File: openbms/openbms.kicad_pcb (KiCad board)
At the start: 4 copper layers, 68.4 x 52.4 mm, 220 parts, among them J1 3-pin JST connector, J2 TagConnect_TC2030, J3 8-pin JST connector, J4 2-pin JST connector, J5 XT60PW-M connector, J6 XT60PW-F connector, J7 7-pin JST connector, Q1 NTMFS5C612NLT1G, Q2 NTMFS5C612NLT1G, Q3 BSS84AKW,115, Q4 2N7002KW, Q5 2N7002KW, Q6 BSS84AKW,115, Q7 2N7002KW, SW1 SW_Push, U1 DMP68D1LVQ-7, U10 DMP68D1LVQ-7, U11 DMN601VK-7, U12 DMN601VK-7, U13 DMN601VK-7, U14 DMN601VK-7, U15 STM32L431CCUx, U16 TCAN3413DRBR, U17 32kbit EEPROM memory, U18 DMP68D1LVQ-7, U19 TPS12000QDGXRQ1, U2 DMP68D1LVQ-7, U20 LMZM23600V3, U22 DMN601VK-7, U3 DMN601VK-7, U4 DMP68D1LVQ-7, U5 ADS131M08xPBS, U6 DMP68D1LVQ-7, U7 DMN601VK-7, U8 DMP68D1LVQ-7, U9 DMP68D1LVQ-7, Y1 8.192MHz, Y2 8MHz

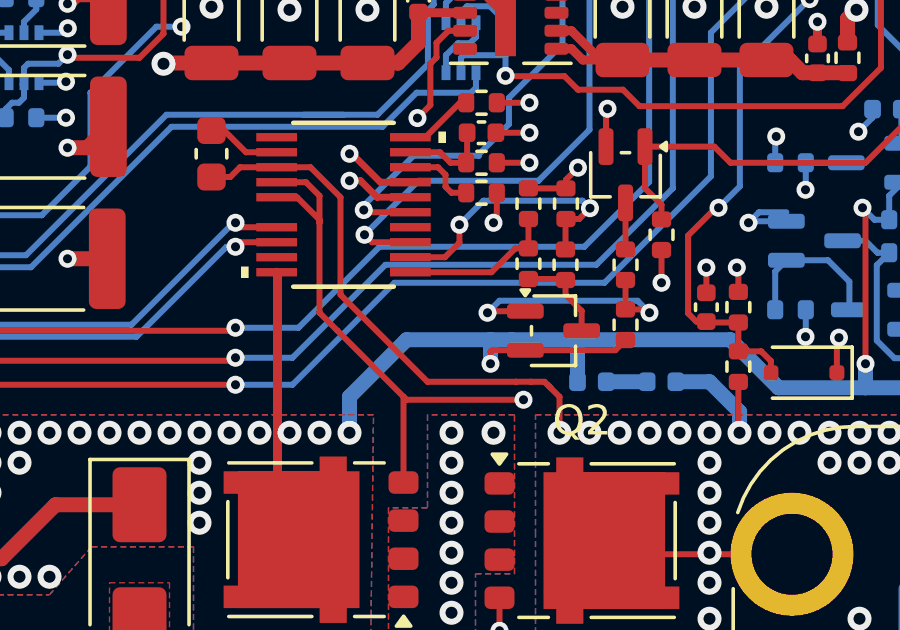
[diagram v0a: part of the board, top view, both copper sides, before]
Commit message: Polygon zone fixed, SRC net in FET fixed
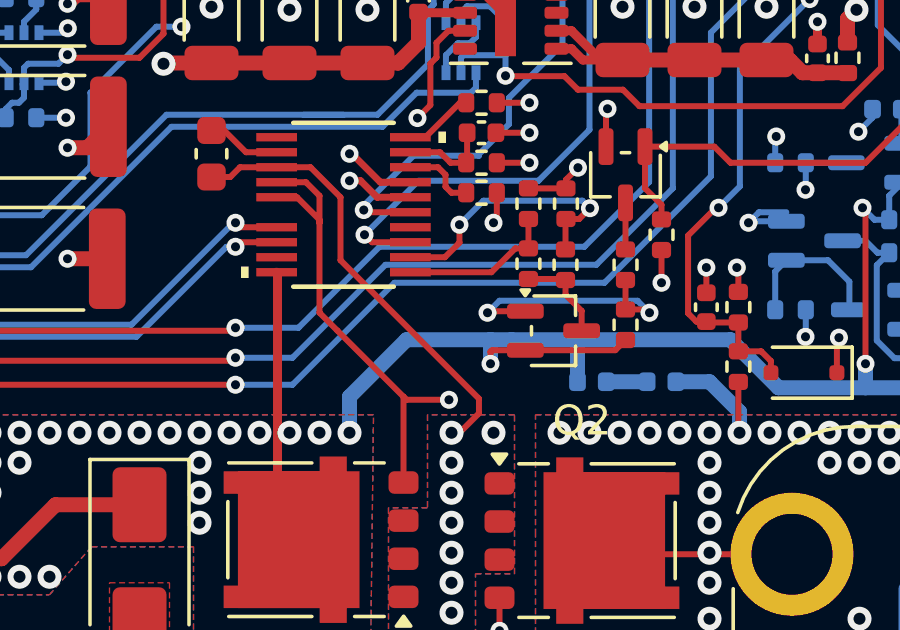
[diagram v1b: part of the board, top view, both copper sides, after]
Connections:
- C33 pad 2: /FETs/SYS_VCC -> Net-(U19-SRC)
- Q1 pad 1: Net-(Q1-S-Pad1) -> Net-(U19-SRC)
- Q1 pad 2: Net-(Q1-S-Pad1) -> Net-(U19-SRC)
- Q1 pad 3: Net-(Q1-S-Pad1) -> Net-(U19-SRC)
- Q2 pad 1: Net-(Q1-S-Pad1) -> Net-(U19-SRC)
- Q2 pad 2: Net-(Q1-S-Pad1) -> Net-(U19-SRC)
- Q2 pad 3: Net-(Q1-S-Pad1) -> Net-(U19-SRC)
- U19 pad 13: /FETs/SYS_VCC -> Net-(U19-SRC)
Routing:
- net /FETs/SYS_VCC: track 43.9 -> 25.7 mm
- net Net-(U19-SRC): track 0.00 -> 15.1 mm, vias 0 -> 10
- net Net-(Q1-S-Pad1): vias 10 -> 0
- added copper zone on B.Cu, net Net-(U19-SRC)
- added copper zone on F.Cu, net Net-(U19-SRC)
- added copper zone on In1.Cu, net Net-(U19-SRC)
- added copper zone on In2.Cu, net Net-(U19-SRC)
- removed copper zone on B.Cu, net Net-(Q1-S-Pad1)
- removed copper zone on F.Cu, net Net-(Q1-S-Pad1)
- removed copper zone on In1.Cu, net Net-(Q1-S-Pad1)
- removed copper zone on In2.Cu, net Net-(Q1-S-Pad1)
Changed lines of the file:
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@@
 	(net 62 "/MCU/NTC")
 	(net 63 "/ADC/BATT_CS_POS")
-	(net 64 "Net-(Q1-S-Pad1)")
+	(net 64 "Net-(U19-SRC)")
 	(net 65 "Net-(Q1-G)")
 	(net 66 "Net-(Q3-D)")
@@
 			(layers "F.Cu" "F.Mask" "F.Paste")
 			(roundrect_rratio 0.25)
-			(net 29 "/FETs/SYS_VCC")
+			(net 64 "Net-(U19-SRC)")
 			(pintype "passive")
 		)
@@
 			(size 1.3589 0.2794)
 			(layers "F.Cu" "F.Mask" "F.Paste")
-			(net 29 "/FETs/SYS_VCC")
+			(net 64 "Net-(U19-SRC)")
 			(pinfunction "SRC")
 			(pintype "output")
@@
 		(sheetname "/FETs/")
 		(sheetfile "FETs.kicad_sch")
+		(zone_connect 2)
 		(attr smd)
 		(fp_line
@@
 			(layers "F.Cu" "F.Mask" "F.Paste")
 			(roundrect_rratio 0.25)
-			(net 64 "Net-(Q1-S-Pad1)")
+			(net 64 "Net-(U19-SRC)")
 			(pinfunction "S")
 			(pintype "passive")
@@
 			(layers "F.Cu" "F.Mask" "F.Paste")
 			(roundrect_rratio 0.25)
-			(net 64 "Net-(Q1-S-Pad1)")
+			(net 64 "Net-(U19-SRC)")
 			(pinfunction "S")
 			(pintype "passive")
@@
 			(layers "F.Cu" "F.Mask" "F.Paste")
 			(roundrect_rratio 0.25)
-			(net 64 "Net-(Q1-S-Pad1)")
+			(net 64 "Net-(U19-SRC)")
 			(pinfunction "S")
 			(pintype "passive")
@@
 			(layers "F.Cu" "F.Mask" "F.Paste")
 			(roundrect_rratio 0.25)
-			(net 64 "Net-(Q1-S-Pad1)")
+			(net 64 "Net-(U19-SRC)")
 			(pinfunction "S")
 			(pintype "passive")
@@
 			(layers "F.Cu" "F.Mask" "F.Paste")
 			(roundrect_rratio 0.25)
-			(net 64 "Net-(Q1-S-Pad1)")
+			(net 64 "Net-(U19-SRC)")
 			(pinfunction "S")
 			(pintype "passive")
@@
 			(layers "F.Cu" "F.Mask" "F.Paste")
 			(roundrect_rratio 0.25)
-			(net 64 "Net-(Q1-S-Pad1)")
+			(net 64 "Net-(U19-SRC)")
 			(pinfunction "S")
 			(pintype "passive")
@@
 	)
 	(segment
-		(start 106.686057 69.1345)
-		(end 106.684057 69.1365)
-		(width 0.2)
-		(layer "F.Cu")
-		(net 29)
-	)
-	(segment
 		(start 110.08225 74.885)
 		(end 109.62725 74.43)
@@
 	)
 	(segment
-		(start 107.8345 69.3355)
-		(end 107.6355 69.1365)
-		(width 0.2)
-		(layer "F.Cu")
-		(net 29)
-	)
-	(segment
-		(start 107.6355 69.1365)
-		(end 107.185943 69.1365)
-		(width 0.2)
-		(layer "F.Cu")
-		(net 29)
-	)
-	(segment
-		(start 100.8345 62.985443)
-		(end 99.834057 61.985)
-		(width 0.2)
-		(layer "F.Cu")
-		(net 29)
-	)
-	(segment
-		(start 108.135 69.636)
-		(end 107.8345 69.3355)
-		(width 0.2)
-		(layer "F.Cu")
-		(net 29)
-	)
-	(segment
-		(start 99.834057 61.985)
-		(end 98.70615 61.985)
-		(width 0.2)
-		(layer "F.Cu")
-		(net 29)
-	)
-	(segment
-		(start 97.1595 62.3105)
-		(end 96.5345 62.3105)
-		(width 0.2)
-		(layer "F.Cu")
-		(net 29)
-	)
-	(segment
-		(start 108.135 70.835)
-		(end 108.135 69.636)
-		(width 0.2)
-		(layer "F.Cu")
-		(net 29)
-	)
-	(segment
 		(start 115.885 74.885)
 		(end 110.08225 74.885)
@@
 	)
 	(segment
-		(start 107.185943 69.1365)
-		(end 107.183943 69.1345)
-		(width 0.2)
-		(layer "F.Cu")
-		(net 29)
-	)
-	(segment
 		(start 128.935 81.135)
 		(end 129.435 80.635)
@@
 	)
 	(segment
-		(start 106.684057 69.1365)
-		(end 103.7355 69.1365)
-		(width 0.2)
-		(layer "F.Cu")
-		(net 29)
-	)
-	(segment
 		(start 126.835 81.135)
 		(end 128.935 81.135)
@@
 	)
 	(segment
-		(start 100.8345 66.2355)
-		(end 100.8345 62.985443)
-		(width 0.2)
-		(layer "F.Cu")
-		(net 29)
-	)
-	(segment
-		(start 98.70615 61.985)
-		(end 97.485 61.985)
-		(width 0.2)
-		(layer "F.Cu")
-		(net 29)
-	)
-	(segment
-		(start 97.485 61.985)
-		(end 97.1595 62.3105)
-		(width 0.2)
-		(layer "F.Cu")
-		(net 29)
-	)
-	(segment
 		(start 123.735 78.035)
 		(end 126.835 81.135)
@@
 	)
 	(segment
-		(start 103.7355 69.1365)
-		(end 100.8345 66.2355)
-		(width 0.2)
-		(layer "F.Cu")
-		(net 29)
-	)
-	(segment
 		(start 114.0968 70.7968)
 		(end 114.135 70.835)
@@
 		(net 29)
 	)
-	(segment
-		(start 107.183943 69.1345)
-		(end 106.686057 69.1345)
-		(width 0.2)
-		(layer "F.Cu")
-		(net 29)
-	)
-	(segment
-		(start 107.8345 69.3355)
-		(end 107.7345 69.2355)
-		(width 0.2)
-		(layer "F.Cu")
-		(net 29)
-	)
 	(via
 		(at 118.135 78.035)
@@
 		(net 63)
 	)
+	(segment
+		(start 100.8345 62.985443)
+		(end 99.834057 61.985)
+		(width 0.2)
+		(layer "F.Cu")
+		(net 64)
+	)
+	(segment
+		(start 97.1595 62.3105)
+		(end 96.5345 62.3105)
+		(width 0.2)
+		(layer "F.Cu")
+		(net 64)
+	)
+	(segment
+		(start 104.535 70.835)
+		(end 104.8015 70.835)
+		(width 0.2)
+		(layer "F.Cu")
+		(net 64)
+	)
+	(segment
+		(start 104.8015 70.835)
+		(end 105.45 70.1865)
+		(width 0.2)
+		(layer "F.Cu")
+		(net 64)
+	)
+	(segment
+		(start 98.70615 61.985)
+		(end 97.485 61.985)
+		(width 0.2)
+		(layer "F.Cu")
+		(net 64)
+	)
+	(segment
+		(start 97.485 61.985)
+		(end 97.1595 62.3105)
+		(width 0.2)
+		(layer "F.Cu")
+		(net 64)
+	)
+	(segment
+		(start 105.45 70.1865)
+		(end 105.45 69.7)
+		(width 0.2)
+		(layer "F.Cu")
+		(net 64)
+	)
+	(segment
+		(start 105.45 69.7)
+		(end 100.8345 65.0845)
+		(width 0.2)
+		(layer "F.Cu")
+		(net 64)
+	)
+	(segment
+		(start 99.834057 61.985)
+		(end 98.70615 61.985)
+		(width 0.2)
+		(layer "F.Cu")
+		(net 64)
+	)
+	(segment
+		(start 100.8345 65.0845)
+		(end 100.8345 62.985443)
+		(width 0.2)
+		(layer "F.Cu")
+		(net 64)
+	)
 	(via
 		(at 104.535 72.835)
@@
 	)
 	(segment
-		(start 103.0355 69.7355)
-		(end 102.935 69.635)
+		(start 100.1345 62.9355)
+		(end 99.683999 62.484999)
 		(width 0.2)
 		(layer "F.Cu")
@@
 	)
 	(segment
-		(start 100.1345 62.9355)
-		(end 99.683999 62.484999)
+		(start 104.45 69.7365)
+		(end 104.449 69.7355)
 		(width 0.2)
 		(layer "F.Cu")
@@
 	)
 	(segment
-		(start 106.935 69.7355)
-		(end 103.0355 69.7355)
-		(width 0.2)
-		(layer "F.Cu")
-		(net 65)
-	)
-	(segment
 		(start 99.683999 62.484999)
 		(end 98.70615 62.484999)
@@
 	)
 	(segment
+		(start 104.449 69.7355)
+		(end 103.0355 69.7355)
+		(width 0.2)
+		(layer "F.Cu")
+		(net 65)
+	)
+	(segment
 		(start 106.135 76.335)
 		(end 106.135 77.435)
@@
 	)
 	(segment
+		(start 103.0355 69.7355)
+		(end 102.935 69.635)
+		(width 0.2)
+		(layer "F.Cu")
+		(net 65)
+	)
+	(segment
 		(start 99.384 62.985)
 		(end 100.1345 63.7355)
@@
 	)
 	(via
-		(at 106.935 69.7355)
+		(at 104.45 69.7365)
 		(size 0.6)
 		(drill 0.3)
@@
 	)
 	(segment
-		(start 106.135 72.335)
-		(end 106.135 77.435)
+		(start 106.135 77.435)
+		(end 106.135 72.265)
+		(width 0.2)
+		(layer "In1.Cu")
+		(net 65)
+	)
+	(segment
+		(start 106.135 72.265)
+		(end 106.85 71.55)
+		(width 0.2)
+		(layer "In1.Cu")
+		(net 65)
+	)
+	(segment
+		(start 106.2365 69.7365)
+		(end 104.45 69.7365)
 		(width 0.2)
 		(layer "In1.Cu")
@@
 	)
 	(segment
-		(start 106.935 69.7355)
-		(end 106.935 71.535)
+		(start 106.85 70.35)
+		(end 106.2365 69.7365)
 		(width 0.2)
 		(layer "In1.Cu")
@@
 	)
 	(segment
-		(start 106.935 71.535)
-		(end 106.135 72.335)
+		(start 106.85 71.55)
+		(end 106.85 70.35)
 		(width 0.2)
 		(layer "In1.Cu")
@@
 		(layers "F.Cu" "B.Cu" "In1.Cu" "In2.Cu")
 		(hatch none 0.5)
-		(priority 2)
 		(connect_pads thru_hole_only
 			(clearance 0.5)
@@
 	(zone
 		(net 64)
-		(net_name "Net-(Q1-S-Pad1)")
+		(net_name "Net-(U19-SRC)")
 		(layers "F.Cu" "B.Cu" "In1.Cu" "In2.Cu")
 		(hatch none 0.5)

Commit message: Green LED part number fixed,  PCB mask color updated, project description updated
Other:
- board text added: "Rev B Q3/2026"
- board text removed: "Rev A Q1/2026"
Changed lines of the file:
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@@
 	(title_block
 		(title "OpenBMS")
-		(date "24-Mar-2026")
-		(rev "Rev A")
+		(date "2026-09-24")
+		(rev "Rev B")
 		(comment 3 "More at openbatt.dev")
 		(comment 4 "Designed by OpenBatt Team")
@@
 			(layer "F.Mask"
 				(type "Top Solder Mask")
-				(color "Black")
+				(color "Purple")
 				(thickness 0.01)
 				(material "Epoxy")
@@
 			(layer "B.Mask"
 				(type "Bottom Solder Mask")
-				(color "Black")
+				(color "Purple")
 				(thickness 0.01)
 				(material "Epoxy")
@@
 			(at 0 -4 0)
 			(layer "F.SilkS")
+			(hide yes)
 			(effects
 				(font
@@
 		(sheetname "/FETs/")
 		(sheetfile "FETs.kicad_sch")
-		(zone_connect 2)
 		(attr smd)
 		(fp_line
@@
 			(pinfunction "D")
 			(pintype "passive")
-			(zone_connect 0)
 			(thermal_bridge_angle 45)
 			(options
@@
 			)
 		)
-		(property "Manufacturer_Part_Number" "LTST-S270KGKT"
+		(property "Manufacturer_Part_Number" "LTST-C190GKT"
 			(at 0 0 270)
 			(unlocked yes)
@@
 			(at 0 -4 180)
 			(layer "F.SilkS")
+			(hide yes)
 			(effects
 				(font
@@
 			(pinfunction "D")
 			(pintype "passive")
-			(zone_connect 0)
 			(thermal_bridge_angle 45)
 			(options
@@
 			(at 0 -4.83 0)
 			(layer "F.SilkS")
+			(hide yes)
 			(effects
 				(font
@@
 		)
 	)
-	(gr_text "Rev A\nQ1/2026"
+	(gr_text "Rev B\nQ3/2026"
 		(at 64.9345 67.6355 270)
 		(layer "B.SilkS")
@@
 		(layers "F.Cu" "B.Cu" "In1.Cu" "In2.Cu")
 		(hatch none 0.5)
+		(priority 2)
 		(connect_pads thru_hole_only
 			(clearance 0.5)
